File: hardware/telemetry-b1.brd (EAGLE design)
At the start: 63.5 x 76.2 mm, 128 parts, among them IC1 COPERNICUSSMD, IC10 TPS70933, IC2 TPS70933, IC4 STM32L073CZT6, IC5 TPS62160, IC6 HX1, IC7 LMP7702, IC9 HIH9131, J1 I2C1, J10 TEMP_BAT, J11 DNP, J12 INSOL, J13 SMA_EDGE, J2 I2C2, J3 SMA_EDGE, J4 USD-SOCKET, J5 BAT, J6 SMA_EDGE, J7 SMA_EDGE, J8 TEMP_GPS, J9 TEMP_HOT, K1 ARE104H, K2 ARE104H, K3 ARE104H, Q1 AO3400A, Q2 AO3400A, Q3 AO3400A, U1 LTC3105, U2 INA219, Y1 32768, Y2 8M

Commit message: Copy filter changes from main Telemetry PCB. Needs a relay rework.
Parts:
- removed C37: 100p, SparkFun-Passives:0805
- removed C38: 47n, SparkFun-Passives:0805
- removed R21: 680, SparkFun-Passives:0805
- R10: value 18K -> 470K
- R16: value 470K -> 820K
- R18: value 10K -> 680K
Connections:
- removed net LP3: C39.1, IC7.5, R27.2
- net A-: no longer C37.2
- net GND: no longer C38.2
- net LP1: now also R27.1; no longer C37.1, R21.1
- net LP2: now also C39.1, IC7.5, R27.2; no longer C38.1, R21.2, R27.1
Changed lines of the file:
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@@
 <element name="C35" library="SparkFun-Passives" package="0805" value="1u" x="-19.05" y="86.36"/>
 <element name="C36" library="SparkFun-Passives" package="0805" value="1u" x="-22.86" y="86.36"/>
-<element name="C37" library="SparkFun-Passives" package="0805" value="100p" x="-26.67" y="86.36"/>
-<element name="C38" library="SparkFun-Passives" package="0805" value="47n" x="-30.48" y="86.36"/>
 <element name="C39" library="SparkFun-Passives" package="0805" value="100p" x="-34.29" y="86.36"/>
 <element name="C4" library="SparkFun-Passives" package="0805" value="0.1u" x="-57.15" y="78.74"/>
@@
 </element>
 <element name="R1" library="SparkFun-Passives" package="0805" value="10K" x="-45.72" y="86.36"/>
-<element name="R10" library="SparkFun-Passives" package="0805" value="18K" x="-76.2" y="86.36"/>
+<element name="R10" library="SparkFun-Passives" package="0805" value="470K" x="-76.2" y="86.36"/>
 <element name="R10\" library="SparkFun-Passives" package="0805" value="430K" x="-80.01" y="86.36"/>
 <element name="R11" library="SparkFun-Passives" package="0805" value="82K" x="-83.82" y="86.36"/>
@@
 <element name="R14" library="SparkFun-Passives" package="0805" value="220" x="-19.05" y="90.17"/>
 <element name="R15" library="SparkFun-Passives" package="0805" value="330" x="-22.86" y="90.17"/>
-<element name="R16" library="SparkFun-Passives" package="0805" value="470K" x="-26.67" y="90.17"/>
+<element name="R16" library="SparkFun-Passives" package="0805" value="820K" x="-26.67" y="90.17"/>
 <element name="R17" library="SparkFun-Passives" package="0805" value="220K" x="-30.48" y="90.17"/>
-<element name="R18" library="SparkFun-Passives" package="0805" value="10K" x="-34.29" y="90.17"/>
+<element name="R18" library="SparkFun-Passives" package="0805" value="680K" x="-34.29" y="90.17"/>
 <element name="R19" library="SparkFun-Passives" package="0805" value="470K" x="-38.1" y="90.17"/>
 <element name="R2" library="SparkFun-Passives" package="0603-ARV" value="10K" x="-62.23" y="67.31"/>
 <element name="R20" library="SparkFun-Passives" package="0805" value="180K" x="-41.91" y="90.17"/>
-<element name="R21" library="SparkFun-Passives" package="0805" value="680" x="-45.72" y="90.17"/>
 <element name="R22" library="SparkFun-Passives" package="0805" value="10K" x="-49.53" y="90.17"/>
 <element name="R23" library="SparkFun-Passives" package="0805" value="4.7K" x="-53.34" y="90.17"/>
@@
 <contactref element="R10" pad="1"/>
 <contactref element="C26" pad="2"/>
-<contactref element="C38" pad="2"/>
 <contactref element="C39" pad="2"/>
 <contactref element="J4" pad="GND1"/>
@@
 <vertex x="13.97" y="63.5"/>
 </polygon>
-<wire x1="57.15" y1="47.625" x2="50.22" y2="47.97" width="0" layer="19" extent="1-1"/>
+<wire x1="49.90914375" y1="70.663153125" x2="52.89" y2="73.24" width="0" layer="19" extent="1-1"/>
+<wire x1="39.867" y1="74.24" x2="49.90914375" y2="70.663153125" width="0" layer="19" extent="1-1"/>
+<wire x1="51.29" y1="60.09" x2="49.90914375" y2="70.663153125" width="0" layer="19" extent="1-1"/>
+<wire x1="45.59" y1="60.09" x2="51.29" y2="60.09" width="0" layer="19" extent="1-1"/>
+<wire x1="57.15" y1="56.515" x2="51.29" y2="60.09" width="0" layer="19" extent="1-1"/>
+<wire x1="57.15" y1="47.625" x2="57.15" y2="56.515" width="0" layer="19" extent="1-1"/>
+<wire x1="50.22" y1="47.97" x2="57.15" y2="47.625" width="0" layer="19" extent="1-1"/>
 <wire x1="43.47" y1="50.22" x2="50.22" y2="47.97" width="0" layer="19" extent="1-1"/>
 <wire x1="41.22" y1="44.97" x2="43.47" y2="50.22" width="0" layer="19" extent="1-1"/>
 <wire x1="47.97" y1="41.22" x2="50.22" y2="47.97" width="0" layer="19" extent="1-1"/>
-<wire x1="8.3058" y1="73.66" x2="8.3058" y2="58.42" width="0" layer="19" extent="1-1"/>
+<wire x1="57.15" y1="38.735" x2="57.15" y2="47.625" width="0" layer="19" extent="1-1"/>
+<wire x1="57.15" y1="29.845" x2="57.15" y2="38.735" width="0" layer="19" extent="1-1"/>
+<wire x1="26.67" y1="73.66" x2="39.867" y2="74.24" width="0" layer="19" extent="1-1"/>
+<wire x1="26.67" y1="72.39" x2="26.67" y2="73.66" width="0" layer="19" extent="1-1"/>
+<wire x1="26.67" y1="57.15" x2="26.67" y2="72.39" width="0" layer="19" extent="1-1"/>
+<wire x1="8.3058" y1="73.66" x2="26.67" y2="73.66" width="0" layer="19" extent="1-1"/>
+<wire x1="8.3058" y1="58.42" x2="8.3058" y2="73.66" width="0" layer="19" extent="1-1"/>
+<wire x1="8.3058" y1="57.15" x2="8.3058" y2="58.42" width="0" layer="19" extent="1-1"/>
+<wire x1="9.525" y1="35.6362" x2="8.3058" y2="57.15" width="0" layer="19" extent="1-1"/>
+<wire x1="12.7" y1="24.13" x2="9.525" y2="35.6362" width="0" layer="19" extent="1-1"/>
 <wire x1="-14.09" y1="78.74" x2="8.3058" y2="73.66" width="0" layer="19" extent="1-1"/>
 <wire x1="-17.9" y1="78.74" x2="-14.09" y2="78.74" width="0" layer="19" extent="1-1"/>
@@
 <wire x1="-25.77" y1="82.55" x2="-21.96" y2="82.55" width="0" layer="19" extent="1-1"/>
 <wire x1="-29.58" y1="82.55" x2="-25.77" y2="82.55" width="0" layer="19" extent="1-1"/>
-<wire x1="-29.58" y1="86.36" x2="-29.58" y2="82.55" width="0" layer="19" extent="1-1"/>
-<wire x1="-33.39" y1="86.36" x2="-29.58" y2="86.36" width="0" layer="19" extent="1-1"/>
+<wire x1="-33.39" y1="82.55" x2="-29.58" y2="82.55" width="0" layer="19" extent="1-1"/>
+<wire x1="-33.39" y1="86.36" x2="-33.39" y2="82.55" width="0" layer="19" extent="1-1"/>
 <wire x1="-37.2" y1="86.36" x2="-33.39" y2="86.36" width="0" layer="19" extent="1-1"/>
-<wire x1="-33.39" y1="82.55" x2="-29.58" y2="82.55" width="0" layer="19" extent="1-1"/>
-<wire x1="-37.2" y1="82.55" x2="-37.2" y2="86.36" width="0" layer="19" extent="1-1"/>
+<wire x1="-37.2" y1="82.55" x2="-33.39" y2="82.55" width="0" layer="19" extent="1-1"/>
 <wire x1="-41.01" y1="82.55" x2="-37.2" y2="82.55" width="0" layer="19" extent="1-1"/>
 <wire x1="-44.82" y1="82.55" x2="-41.01" y2="82.55" width="0" layer="19" extent="1-1"/>
@@
 <wire x1="-29.33" y1="78.74" x2="-25.52" y2="78.74" width="0" layer="19" extent="1-1"/>
 <wire x1="-40.76" y1="78.74" x2="-41.01" y2="82.55" width="0" layer="19" extent="1-1"/>
-<wire x1="-31.38" y1="90.17" x2="-29.58" y2="86.36" width="0" layer="19" extent="1-1"/>
 <wire x1="-42.81" y1="86.36" x2="-41.01" y2="82.55" width="0" layer="19" extent="1-1"/>
 <wire x1="-42.81" y1="90.17" x2="-42.81" y2="86.36" width="0" layer="19" extent="1-1"/>
@@
 <wire x1="-84.72" y1="86.36" x2="-82.92" y2="82.55" width="0" layer="19" extent="1-1"/>
 <wire x1="-88.53" y1="86.36" x2="-84.72" y2="86.36" width="0" layer="19" extent="1-1"/>
+<wire x1="-31.38" y1="90.17" x2="-33.39" y2="86.36" width="0" layer="19" extent="1-1"/>
 <wire x1="-58.05" y1="86.36" x2="-60.06" y2="82.55" width="0" layer="19" extent="1-1"/>
 <wire x1="-43.942" y1="73.66" x2="-44.82" y2="78.74" width="0" layer="19" extent="1-1"/>
@@
 <signal name="A-">
 <contactref element="R10" pad="2"/>
-<contactref element="C37" pad="2"/>
 <contactref element="R18" pad="1"/>
 <contactref element="IC7" pad="2"/>
-<wire x1="-35.19" y1="90.17" x2="-25.77" y2="86.36" width="0" layer="19" extent="1-1"/>
 <wire x1="-75.3" y1="86.36" x2="-35.19" y2="90.17" width="0" layer="19" extent="1-1"/>
-<wire x1="12.065" y1="35.6362" x2="-25.77" y2="86.36" width="0" layer="19" extent="1-1"/>
+<wire x1="12.065" y1="35.6362" x2="-35.19" y2="90.17" width="0" layer="19" extent="1-1"/>
 </signal>
 <signal name="A+">
@@
 <contactref element="IC7" pad="1"/>
 <contactref element="R18" pad="2"/>
-<contactref element="C37" pad="1"/>
-<contactref element="R21" pad="1"/>
-<wire x1="-33.39" y1="90.17" x2="-27.57" y2="86.36" width="0" layer="19" extent="1-1"/>
-<wire x1="-46.62" y1="90.17" x2="-33.39" y2="90.17" width="0" layer="19" extent="1-1"/>
-<wire x1="13.335" y1="35.6362" x2="-27.57" y2="86.36" width="0" layer="19" extent="1-1"/>
+<contactref element="R27" pad="1"/>
+<wire x1="-69.48" y1="90.17" x2="-33.39" y2="90.17" width="0" layer="19" extent="1-1"/>
+<wire x1="13.335" y1="35.6362" x2="-33.39" y2="90.17" width="0" layer="19" extent="1-1"/>
 </signal>
 <signal name="LP2">
-<contactref element="C38" pad="1"/>
-<contactref element="R21" pad="2"/>
-<contactref element="R27" pad="1"/>
-<wire x1="-44.82" y1="90.17" x2="-31.38" y2="86.36" width="0" layer="19" extent="1-1"/>
-<wire x1="-69.48" y1="90.17" x2="-44.82" y2="90.17" width="0" layer="19" extent="1-1"/>
-</signal>
-<signal name="LP3">
+<contactref element="IC7" pad="5"/>
+<contactref element="C39" pad="1"/>
 <contactref element="R27" pad="2"/>
-<contactref element="C39" pad="1"/>
-<contactref element="IC7" pad="5"/>
 <wire x1="-67.68" y1="90.17" x2="-35.19" y2="86.36" width="0" layer="19" extent="1-1"/>
 <wire x1="9.525" y1="30.4038" x2="-35.19" y2="86.36" width="0" layer="19" extent="1-1"/>

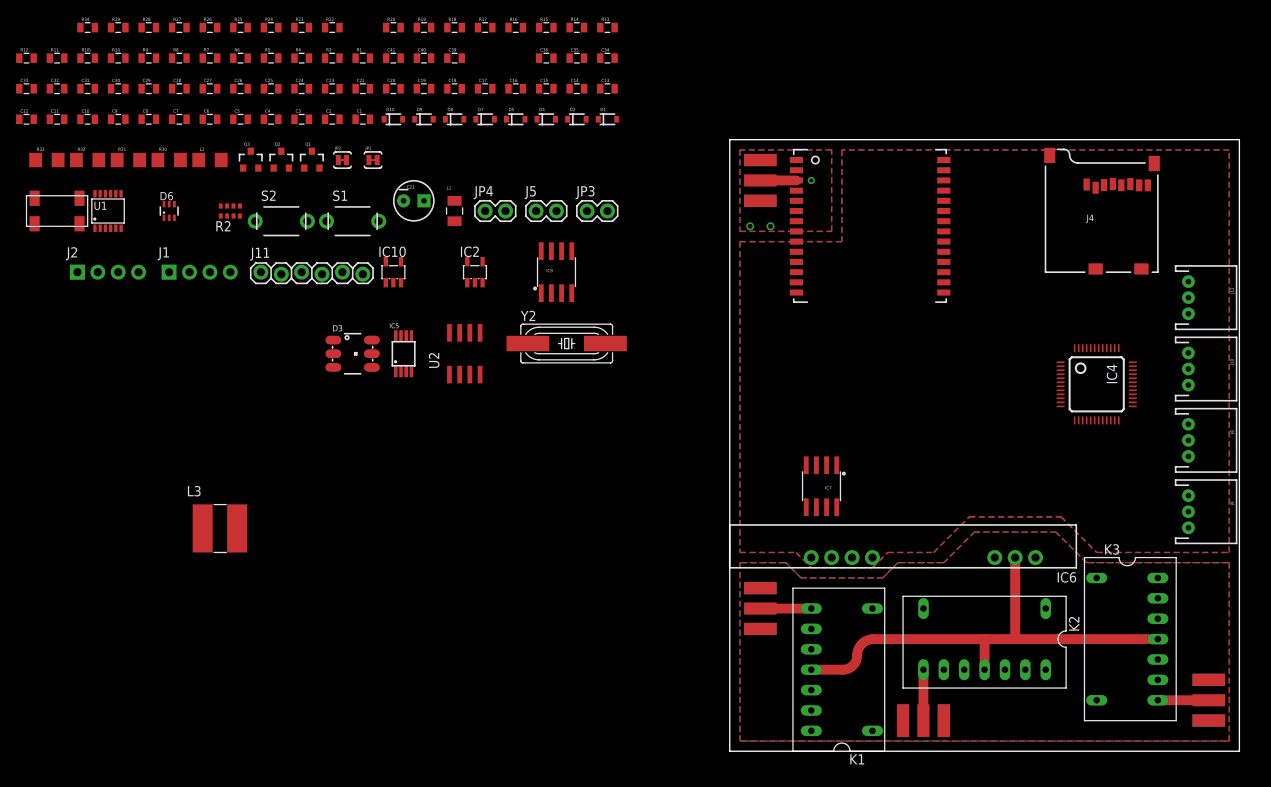
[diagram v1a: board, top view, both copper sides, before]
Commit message: Strip unnecessary relay, and fix most RF stubs
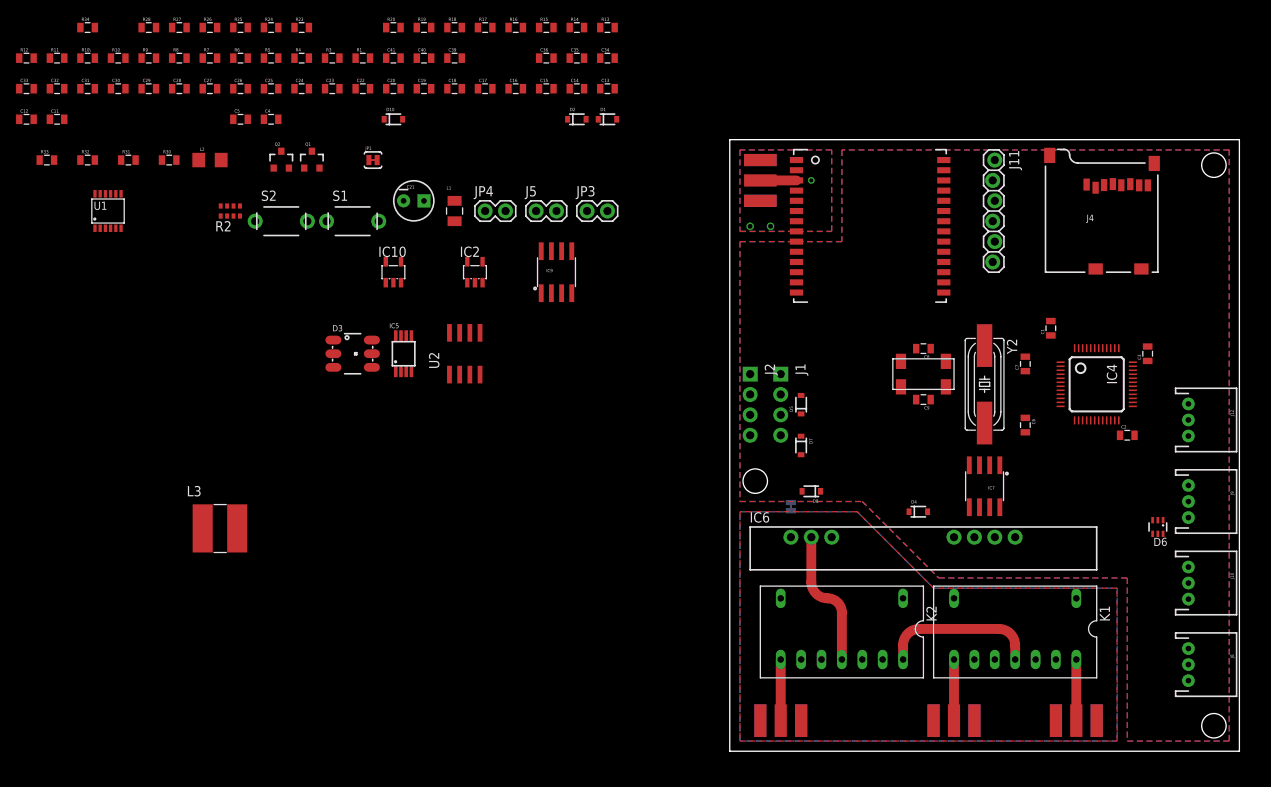
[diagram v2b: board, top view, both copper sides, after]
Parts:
- removed C10: 0.1u, SparkFun-Passives:0805
- removed D9: BAT20J, SparkFun-DiscreteSemi:SOD-323
- removed K3: ARE104H, HAB:RFDIL14
- removed Q3: AO3400A, SparkFun-DiscreteSemi:SOT23-3
- removed R22: 10K, SparkFun-Passives:0805
- removed R29: 180K, SparkFun-Passives:0805
- R30, R31, R32, R33: device SparkFun-Passives:1206 -> SparkFun-Passives:0805
- moved D6 129.3 mm to (53.3, 27.9), turned to 180 degrees
- moved Y1 109.8 mm to (24.1, 47.0), turned to 180 degrees
- moved C7 109.7 mm to (36.8, 48.3), turned to 90 degrees
- moved C3 109.4 mm to (52.1, 49.5), turned to 90 degrees
- moved C6 108.5 mm to (36.8, 40.6), turned to 270 degrees
- moved C2 106.6 mm to (49.5, 39.4)
- moved C9 106.2 mm to (24.1, 43.8), turned to 180 degrees
- moved C8 100.7 mm to (24.1, 50.2), turned to 180 degrees
- moved J11 92.5 mm to (33.0, 73.7), turned to 270 degrees
- moved C1 89.6 mm to (40.0, 52.7), turned to 90 degrees
- moved J2 84.8 mm to (2.54, 47.0), turned to 270 degrees
- moved J1 77.3 mm to (6.35, 47.0), turned to 270 degrees
- moved JP2 70.6 mm to (7.62, 30.5), flipped to the bottom, turned to 90 degrees
- moved D4 67.4 mm to (23.5, 29.8)
- moved D8 64.2 mm to (10.2, 32.4), turned to 180 degrees
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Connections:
- removed net N$3: Q3.1, R22.2, R29.2
- removed net RD2: D9.A, K3.7, Q3.3
- removed net RS2: IC4.25, R22.1
- new net RF_STUB: K1.11, K2.14
- net 3.3V: no longer C10.1
- net 5V: no longer D9.C, K3.1
- net GND: no longer C10.2, Q3.2, R29.1
- net RF2: now also K1.14; no longer K3.8
- net RF_HX1: no longer K1.11, K3.11
- net RGND: no longer K3.10, K3.12, K3.13, K3.9
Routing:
- net RF_HX1: track 58.7 -> 16.8 mm
- net RF_STUB: track 0.00 -> 19.2 mm
- net RF2: track 6.35 -> 7.62 mm
- net RF1: track 6.35 -> 7.62 mm
- net RF0: track 6.35 -> 7.62 mm

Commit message: Work on beta PCB layout. Most placement is done, probably will have no room for the HIH (or put it on the back).
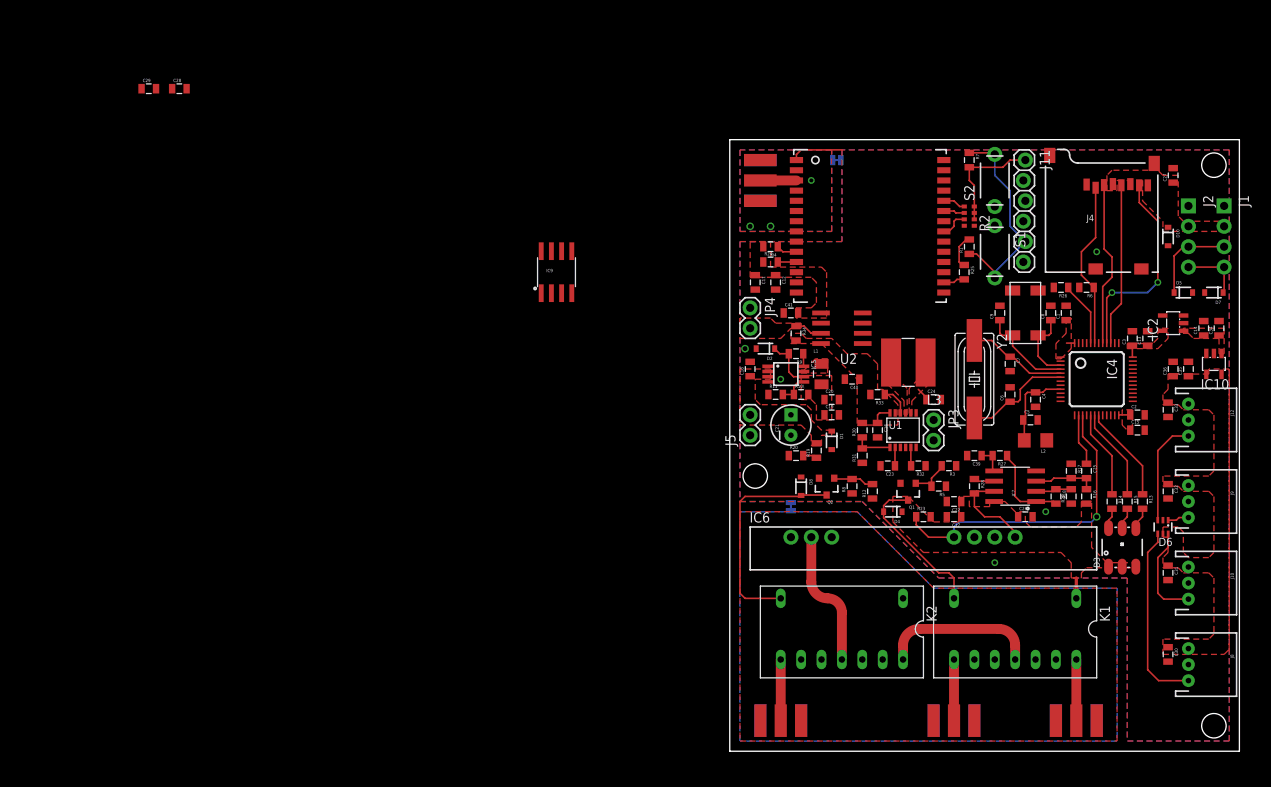
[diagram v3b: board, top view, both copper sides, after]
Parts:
- removed R10: 470K, SparkFun-Passives:0805
- added R29: 470K, SparkFun-Passives:0805
- moved C30 148.6 mm to (54.6, 12.1), turned to 270 degrees
- moved C33 147.8 mm to (54.6, 42.5), turned to 270 degrees
- moved C31 147.5 mm to (54.6, 22.2), turned to 270 degrees
- moved C32 147.2 mm to (54.6, 32.4), turned to 270 degrees
- moved C27 120.5 mm to (55.2, 71.8), turned to 90 degrees
- moved R12 118.4 mm to (17.8, 32.4), turned to 90 degrees
- moved R28 117.7 mm to (30.5, 33.0), turned to 270 degrees
- moved R27 115.3 mm to (33.7, 36.8), turned to 180 degrees
- moved C25 112.2 mm to (44.5, 34.9), turned to 270 degrees
- moved C26 111.4 mm to (36.8, 29.2)
- moved R26 110.9 mm to (41.3, 57.8), turned to 180 degrees
- moved R32 110.3 mm to (23.5, 35.6), turned to 180 degrees
- moved R6 109.2 mm to (44.5, 57.8), turned to 180 degrees
- moved L2 108.6 mm to (38.1, 38.7), turned to 180 degrees
- moved R33 107.5 mm to (18.4, 44.5), turned to 180 degrees
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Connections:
- net N$1 renamed Q2B
- net N$2 renamed Q1B
- net N$4 renamed BVOUT
- net A-: now also R29.2; no longer R10.2
- net CSSD: now also IC4.43; no longer IC4.38
- net GND: now also R29.1; no longer R10.1
- net RS0: now also IC4.27; no longer IC4.43
- net RS1: now also IC4.28; no longer IC4.42
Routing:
- net HXEN: track 0.00 -> 39.3 mm, vias 0 -> 1
- net RD1: track 0.00 -> 27.9 mm
- net MISO: track 0.00 -> 25.9 mm, vias 0 -> 2
- net TEMPG: track 0.00 -> 23.1 mm
- net 3.3V: track 0.00 -> 22.0 mm
- net CSSD: track 0.00 -> 20.8 mm
- net MOSI: track 0.00 -> 20.6 mm
- net SCK: track 0.00 -> 20.2 mm
- net RD0: track 0.00 -> 19.3 mm
- net BTN: track 0.00 -> 15.7 mm
- net OSC_OUT: track 0.00 -> 13.6 mm
- net INSOL: track 0.00 -> 13.2 mm
- net OSC_IN: track 0.00 -> 12.4 mm
- net LEDB: track 0.00 -> 12.1 mm
- net TEMPB: track 0.00 -> 12.0 mm
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- added copper zone on layer 1, net +9V
- added copper zone on layer 1, net 3.3V
- added copper zone on layer 1, net 5V
- added copper zone on layer 1, net BVOUT
- added copper zone on layer 1, net SVIN
- added copper zone on layer 1, net SVOUT
- added copper zone on layer 1, net SW
- added copper zone on layer 1, net SW5
- added copper zone on layer 1, net VS
